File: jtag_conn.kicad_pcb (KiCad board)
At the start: 2 copper layers, 39.3 x 28.7 mm, 9 parts, among them J1 CONN_10X2, J2 CONN_5X2, J3 CONN_1X1, J4 CONN_1X1, J5 CONN_5X2, J6 CONN_6X1, J7 CONN_5X1, J8 CONN_6X1, J9 CONN_5X1

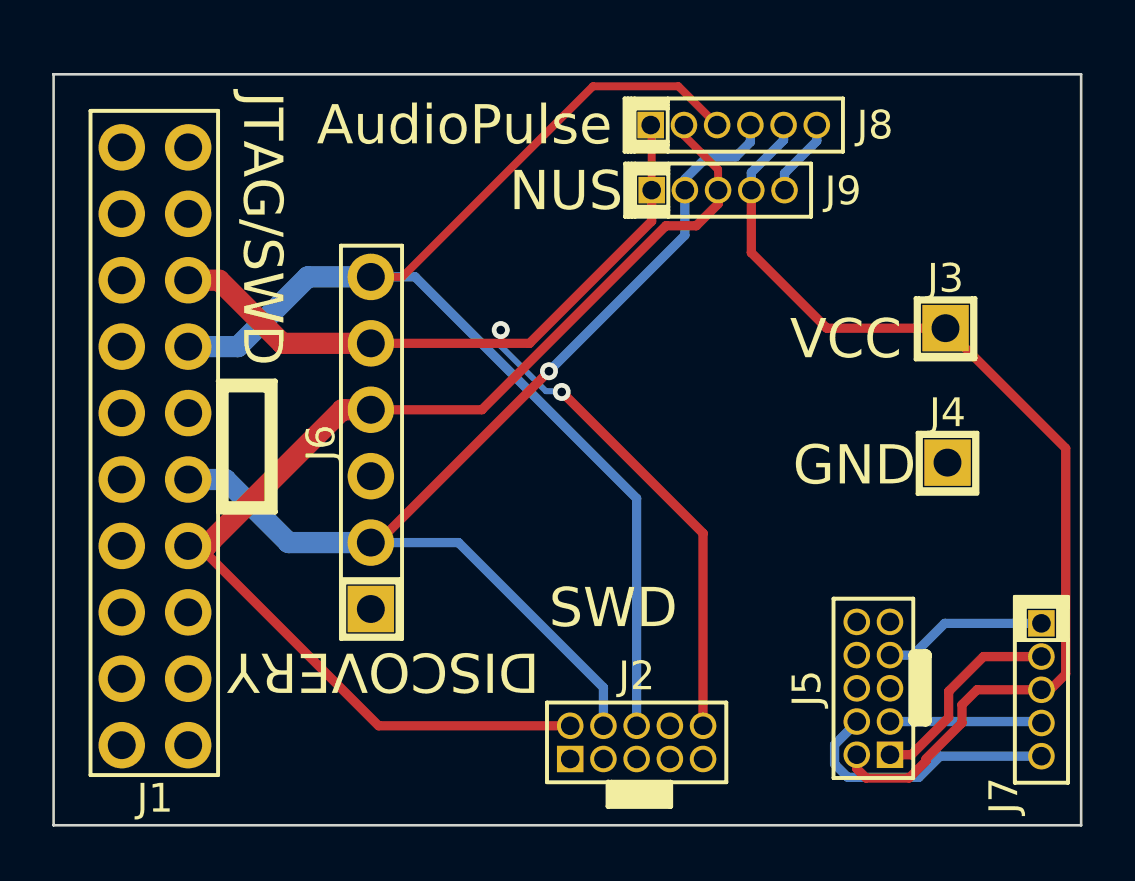
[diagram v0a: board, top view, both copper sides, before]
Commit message: Printed r1a
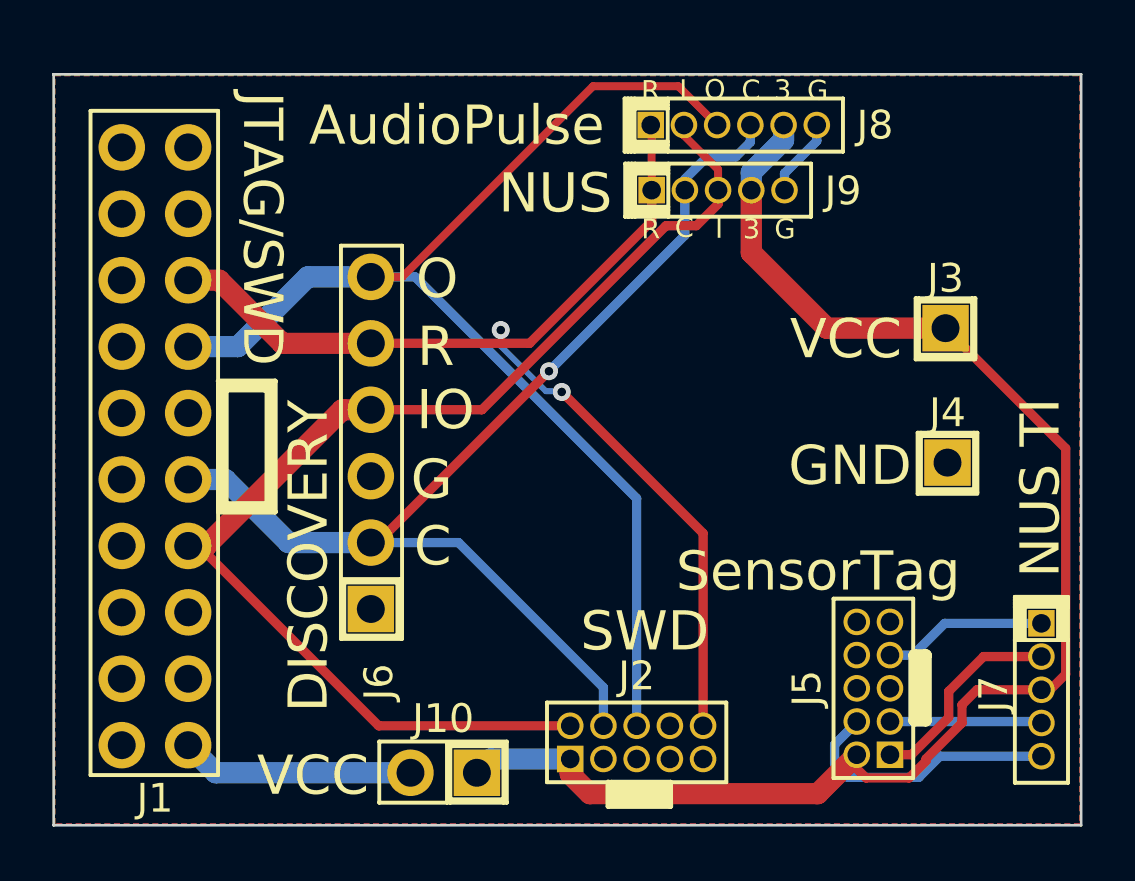
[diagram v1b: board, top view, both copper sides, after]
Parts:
- added J10: CONN_2X1, HDR_2X1_100MIL_THRU, F.Cu at (51.6, 59.8)
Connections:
- J1 pad 1: /VCC -> /VCC_JTAG
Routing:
- net /VCC: track 39.9 -> 56.2 mm
- net /VCC_JTAG: track 0.00 -> 8.94 mm
- added copper zone on B.Cu, net /GND
- added copper zone on F.Cu, net /GND
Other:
- board text added: "3"
- board text added: "BRN"
- board text added: "C"
- board text added: "G"
- board text added: "I"
- board text added: "IO"
- board text added: "NUS TI"
- board text added: "O"
- board text added: "R"
- board text added: "SensorTag"
- board text added: "r1a"
